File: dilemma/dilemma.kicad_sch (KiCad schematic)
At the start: 64 parts, among them J1 S3B-PH-SM4-TB(LF)(SN), J2 Serial, J3 BATTERY_CONN_DEANS, J5 S3B-PH-SM4-TB(LF)(SN), J7 trackball, SW1 SW_Push, SW10 SW_Push, SW11 SW_Push, SW12 SW_Push, SW13 SW_Push, SW14 SW_Push, SW15 SW_Push, SW16 SW_Push, SW17 SW_Push, SW2 SW_Push, SW26 SW_SPST, SW3 SW_Push, SW37 SW_SPST, SW4 SW_Push, SW5 SW_Push, SW6 SW_Push, SW7 SW_Push, SW8 SW_Push, SW9 SW_Push, U2 eliteC

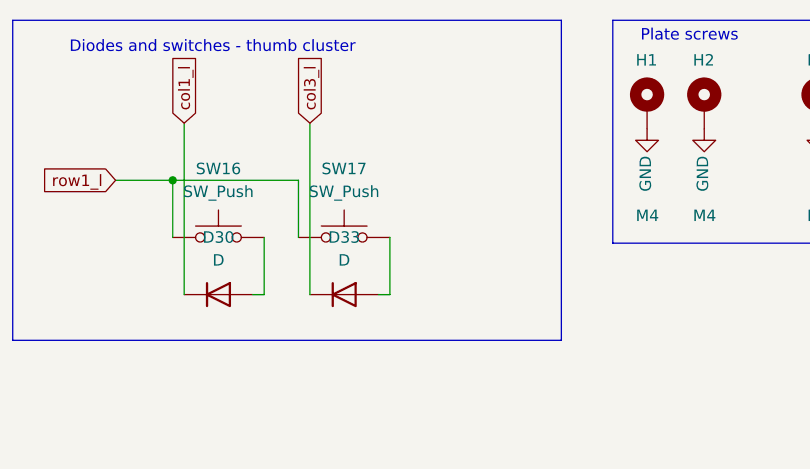
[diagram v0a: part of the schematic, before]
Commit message: Add thumb key
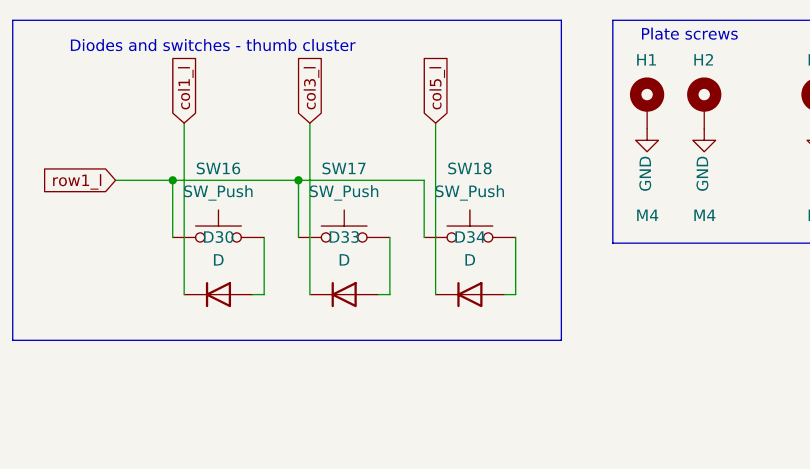
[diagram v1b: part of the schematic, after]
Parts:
- added D34: D, local-libraries:D_1206_handsolder_reversible, symbol Device:D
- added SW18: SW_Push, local-libraries:SW_MX_choc, symbol Switch:SW_Push
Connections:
- net col5_l: now also D34.1 (K)
- net row1_l: now also SW18.1
- new net: D34.2 (A), SW18.2
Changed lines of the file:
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@@
   (junction (at 109.22 45.72) (diameter 0) (color 0 0 0 0)
+  )
+  (junction (at 226.06 40.64) (diameter 0) (color 0 0 0 0)
   )
   (junction (at 212.09 40.64) (diameter 0) (color 0 0 0 0)
@@
     (stroke (width 0) (type default) (color 0 0 0 0))
   )
+  (wire (pts (xy 250.19 46.99) (xy 250.19 53.34))
+    (stroke (width 0) (type solid) (color 0 0 0 0))
+  )
   (wire (pts (xy 55.88 35.56) (xy 82.55 35.56))
     (stroke (width 0) (type default) (color 0 0 0 0))
@@
     (stroke (width 0) (type default) (color 0 0 0 0))
   )
+  (wire (pts (xy 250.19 53.34) (xy 248.92 53.34))
+    (stroke (width 0) (type solid) (color 0 0 0 0))
+  )
   (wire (pts (xy 308.61 111.76) (xy 311.785 111.76))
     (stroke (width 0) (type default) (color 0 0 0 0))
@@
     (stroke (width 0) (type default) (color 0 0 0 0))
   )
+  (wire (pts (xy 241.3 34.29) (xy 241.3 53.34))
+    (stroke (width 0) (type solid) (color 0 0 0 0))
+  )
+  (wire (pts (xy 226.06 40.64) (xy 240.03 40.64))
+    (stroke (width 0) (type solid) (color 0 0 0 0))
+  )
   (wire (pts (xy 154.94 48.26) (xy 158.75 48.26))
     (stroke (width 0) (type default) (color 0 0 0 0))
@@
   (wire (pts (xy 128.27 58.42) (xy 132.08 58.42))
     (stroke (width 0) (type default) (color 0 0 0 0))
+  )
+  (wire (pts (xy 240.03 40.64) (xy 240.03 46.99))
+    (stroke (width 0) (type solid) (color 0 0 0 0))
   )
   (wire (pts (xy 128.27 38.1) (xy 132.08 38.1))
@@
     )
   )
+  (global_label "col5_l" (shape input) (at 241.3 34.29 90)
+    (effects (font (size 1.27 1.27)) (justify left))
+    (property "Intersheet References" "${INTERSHEET_REFS}" (id 0) (at 96.52 3.81 0)
+      (effects (font (size 1.27 1.27)) hide)
+    )
+  )
   (global_label "bat_sw_l" (shape input) (at 177.8 99.06 180)
     (effects (font (size 1.27 1.27)) (justify right))
@@
     (pin "2")
   )
+  (symbol (lib_id "Device:D") (at 245.11 53.34 0) (unit 1)
+    (in_bom yes) (on_board yes)
+    (property "Reference" "D34" (id 0) (at 245.11 46.99 0))
+    (property "Value" "D" (id 1) (at 245.11 49.53 0))
+    (property "Footprint" "local-libraries:D_1206_handsolder_reversible" (id 2) (at 245.11 53.34 0)
+      (effects (font (size 1.27 1.27)) hide)
+    )
+    (property "Datasheet" "~" (id 3) (at 245.11 53.34 0)
+      (effects (font (size 1.27 1.27)) hide)
+    )
+    (pin "1")
+    (pin "2")
+  )
   (symbol (lib_id "Mechanical:MountingHole_Pad") (at 320.04 32.385 0) (unit 1)
     (in_bom yes) (on_board yes)
@@
     )
     (property "JLCPCB Part" "C26033" (id 5) (at 55.372 152.4 0)
+      (effects (font (size 1.27 1.27)) hide)
+    )
+    (pin "1")
+    (pin "2")
+  )
+  (symbol (lib_id "Switch:SW_Push") (at 245.11 46.99 0) (unit 1)
+    (in_bom yes) (on_board yes)
+    (property "Reference" "SW18" (id 0) (at 245.11 39.37 0))
+    (property "Value" "SW_Push" (id 1) (at 245.11 41.91 0))
+    (property "Footprint" "local-libraries:SW_MX_choc" (id 2) (at 245.11 41.91 0)
+      (effects (font (size 1.27 1.27)) hide)
+    )
+    (property "Datasheet" "~" (id 3) (at 245.11 41.91 0)
       (effects (font (size 1.27 1.27)) hide)
     )
@@
       (reference "D33") (unit 1) (value "D") (footprint "local-libraries:D_1206_handsolder_reversible")
     )
+    (path "/14dac5a2-a0ff-4444-afb5-3f69e91ff7db"
+      (reference "D34") (unit 1) (value "D") (footprint "local-libraries:D_1206_handsolder_reversible")
+    )
     (path "/66749c6a-b16f-43be-bab1-76caa7a8a44a"
       (reference "H1") (unit 1) (value "M4") (footprint "local-libraries:MountingHole_3mm_Pad_thin")
@@
       (reference "SW17") (unit 1) (value "SW_Push") (footprint "local-libraries:SW_MX_choc")
     )
+    (path "/2c60993d-fff3-4952-b82a-c33bf7f0fa97"
+      (reference "SW18") (unit 1) (value "SW_Push") (footprint "local-libraries:SW_MX_choc")
+    )
     (path "/bc6fb766-b233-4d2e-bea0-ce056a378236"

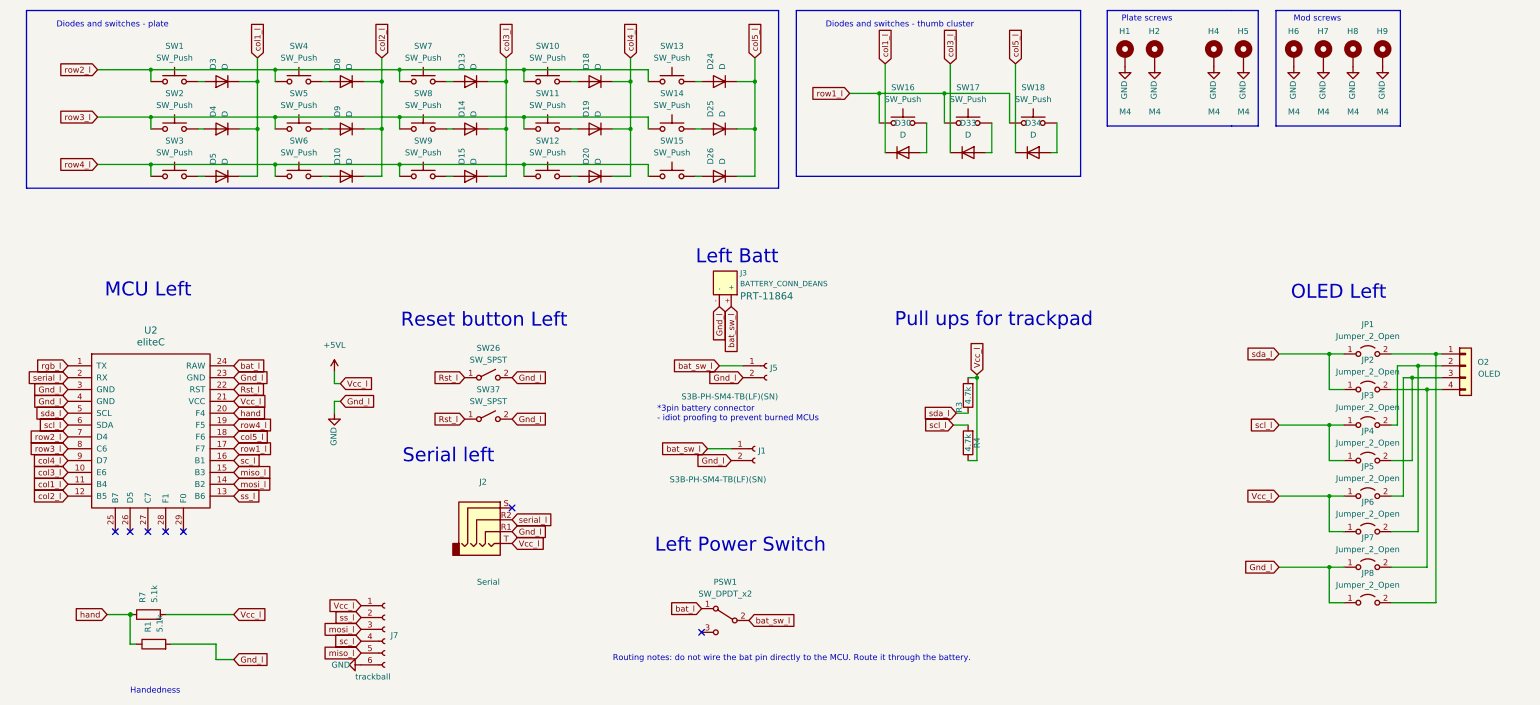
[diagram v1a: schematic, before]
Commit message: Create place for col6
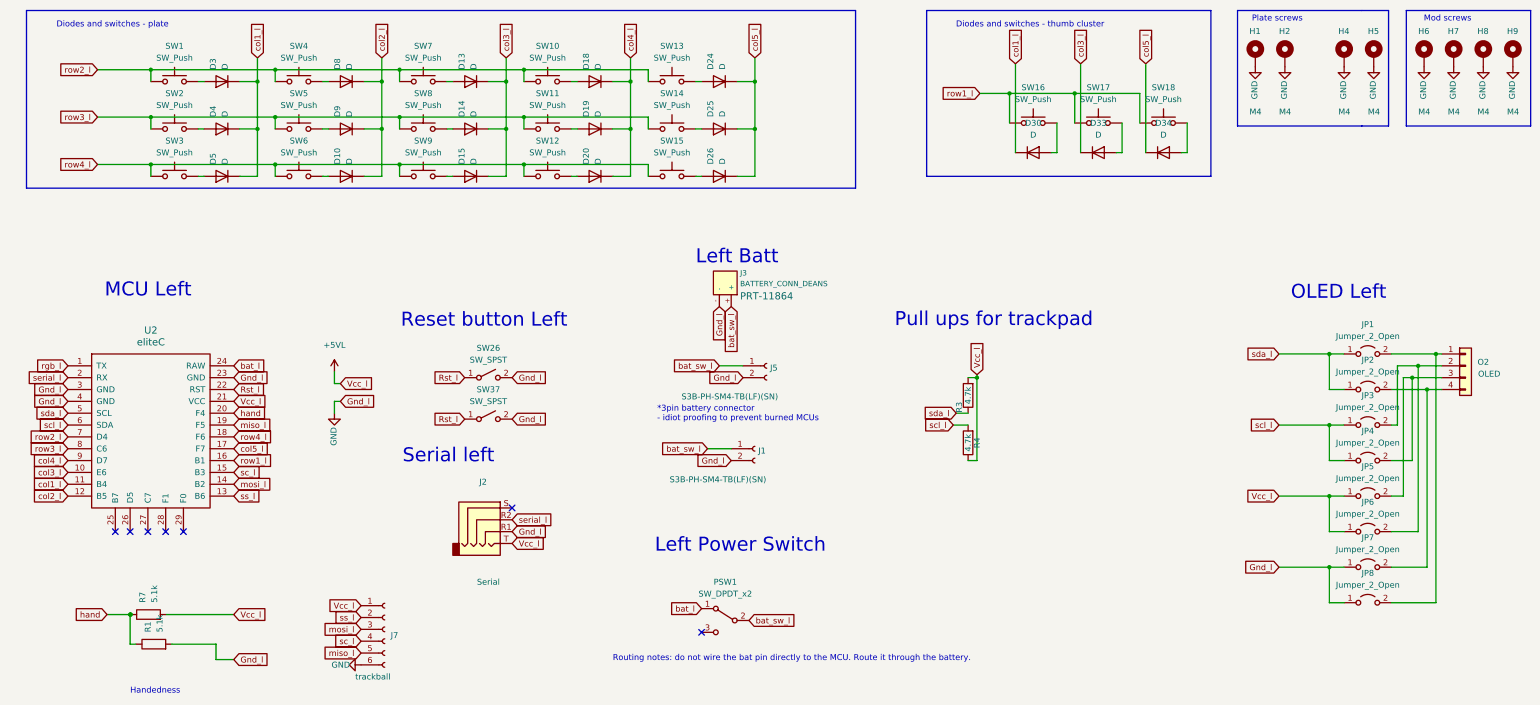
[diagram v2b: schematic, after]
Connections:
- net col5_l: now also U2.17 (F7); no longer U2.18 (F6)
- net miso_l: now also U2.19 (F5); no longer U2.15 (B3)
- net row1_l: now also U2.16 (B1); no longer U2.17 (F7)
- net row4_l: now also U2.18 (F6); no longer U2.19 (F5)
- net sc_l: now also U2.15 (B3); no longer U2.16 (B1)
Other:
- moved on the sheet: D30, D33, D34, H1, H2, H4, H5, H6, H7, H8, H9, SW16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

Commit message: Add 6th column
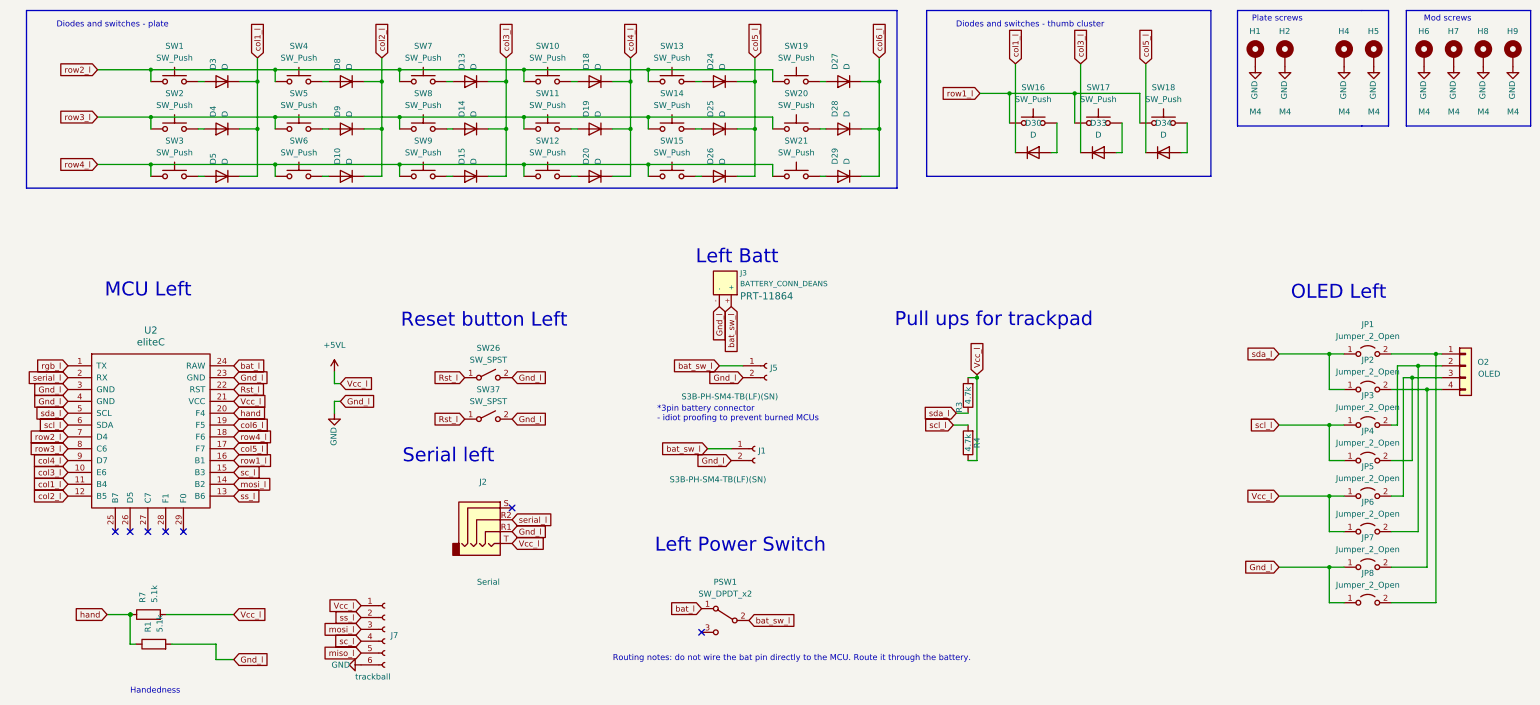
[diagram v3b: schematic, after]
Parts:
- added D27, D28, D29: D, local-libraries:D_1206_handsolder_reversible, symbol Device:D
- added SW19, SW20, SW21: SW_Push, local-libraries:SW_MX_choc, symbol Switch:SW_Push
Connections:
- net miso_l: no longer U2.19 (F5)
- net row2_l: now also SW19.1
- net row3_l: now also SW20.1
- net row4_l: now also SW21.1
- new net: D29.2 (A), SW21.2
- new net: D27.2 (A), SW19.2
- new net: D28.2 (A), SW20.2
- new net col6_l: D27.1 (K), D28.1 (K), D29.1 (K), U2.19 (F5)

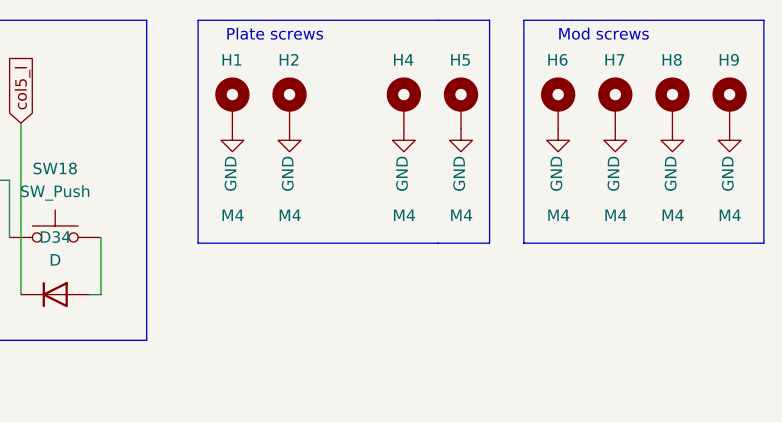
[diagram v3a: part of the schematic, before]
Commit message: Remove H4 hole
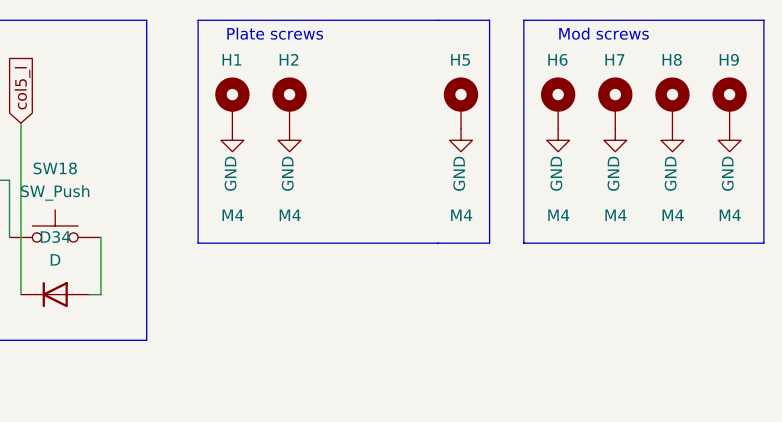
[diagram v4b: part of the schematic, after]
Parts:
- removed H4: M4, local-libraries:MountingHole_3mm_Pad_thin, symbol Mechanical:MountingHole_Pad
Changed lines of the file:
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@@
     (pin "2")
-  )
-  (symbol (lib_id "Mechanical:MountingHole_Pad") (at 311.785 32.385 0) (unit 1)
-    (in_bom yes) (on_board yes)
-    (property "Reference" "H4" (id 0) (at 310.515 27.305 0)
-      (effects (font (size 1.27 1.27)) (justify left))
-    )
-    (property "Value" "M4" (id 1) (at 310.515 44.577 0)
-      (effects (font (size 1.27 1.27)) (justify left))
-    )
-    (property "Footprint" "local-libraries:MountingHole_3mm_Pad_thin" (id 2) (at 311.785 32.385 0)
-      (effects (font (size 1.27 1.27)) hide)
-    )
-    (property "Datasheet" "~" (id 3) (at 311.785 32.385 0)
-      (effects (font (size 1.27 1.27)) hide)
-    )
-    (pin "1")
   )
   (symbol (lib_id "Switch:SW_Push") (at 114.3 48.26 0) (unit 1)
@@
     (pin "2")
   )
-  (symbol (lib_id "power:GND") (at 311.785 34.925 0) (unit 1)
-    (in_bom yes) (on_board yes)
-    (property "Reference" "#PWR0103" (id 0) (at 311.785 41.275 0)
-      (effects (font (size 1.27 1.27)) hide)
-    )
-    (property "Value" "GND" (id 1) (at 311.629 41.9099 90)
-      (effects (font (size 1.27 1.27)) (justify left))
-    )
-    (property "Footprint" "" (id 2) (at 311.785 34.925 0)
-      (effects (font (size 1.27 1.27)) hide)
-    )
-    (property "Datasheet" "" (id 3) (at 311.785 34.925 0)
-      (effects (font (size 1.27 1.27)) hide)
-    )
-    (pin "1")
-  )
   (symbol (lib_id "power:GND") (at 328.93 34.925 0) (unit 1)
     (in_bom yes) (on_board yes)
@@
       (reference "#PWR0102") (unit 1) (value "GND") (footprint "")
     )
-    (path "/fb97fa38-e913-4813-bbb6-ec56f9359020"
-      (reference "#PWR0103") (unit 1) (value "GND") (footprint "")
-    )
     (path "/9a573a5f-16ed-4bac-a9aa-25b5d86e5dd3"
       (reference "#PWR0104") (unit 1) (value "GND") (footprint "")
@@
       (reference "H2") (unit 1) (value "M4") (footprint "local-libraries:MountingHole_3mm_Pad_thin")
     )
-    (path "/eab541c6-214e-4bdc-a65e-96cf56f5a486"
-      (reference "H4") (unit 1) (value "M4") (footprint "local-libraries:MountingHole_3mm_Pad_thin")
-    )
     (path "/2da60390-ff21-4437-82a4-3e8bcdc893cf"

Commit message: Revert "Remove H4 hole"
This reverts commit eafe3389c8530ed03ec8ad130b3a2f53ccdd09a2.
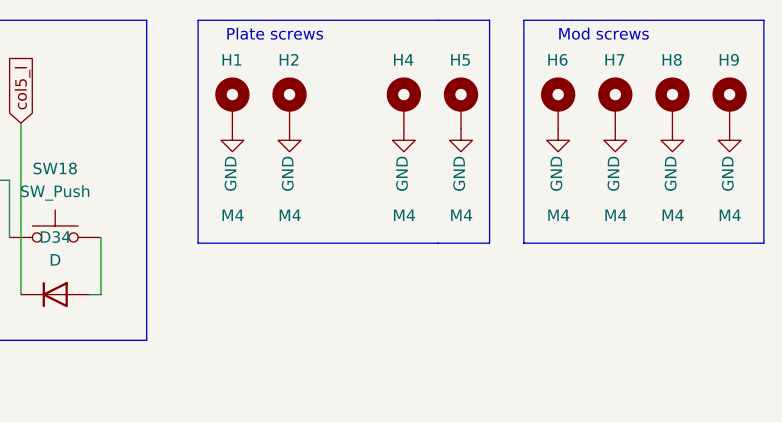
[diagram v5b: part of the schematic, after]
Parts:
- added H4: M4, local-libraries:MountingHole_3mm_Pad_thin, symbol Mechanical:MountingHole_Pad
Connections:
- net GND: now also H4.1
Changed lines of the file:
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@@
     (pin "2")
+  )
+  (symbol (lib_id "Mechanical:MountingHole_Pad") (at 311.785 32.385 0) (unit 1)
+    (in_bom yes) (on_board yes)
+    (property "Reference" "H4" (id 0) (at 310.515 27.305 0)
+      (effects (font (size 1.27 1.27)) (justify left))
+    )
+    (property "Value" "M4" (id 1) (at 310.515 44.577 0)
+      (effects (font (size 1.27 1.27)) (justify left))
+    )
+    (property "Footprint" "local-libraries:MountingHole_3mm_Pad_thin" (id 2) (at 311.785 32.385 0)
+      (effects (font (size 1.27 1.27)) hide)
+    )
+    (property "Datasheet" "~" (id 3) (at 311.785 32.385 0)
+      (effects (font (size 1.27 1.27)) hide)
+    )
+    (pin "1")
   )
   (symbol (lib_id "Switch:SW_Push") (at 114.3 48.26 0) (unit 1)
@@
     (pin "2")
   )
+  (symbol (lib_id "power:GND") (at 311.785 34.925 0) (unit 1)
+    (in_bom yes) (on_board yes)
+    (property "Reference" "#PWR0103" (id 0) (at 311.785 41.275 0)
+      (effects (font (size 1.27 1.27)) hide)
+    )
+    (property "Value" "GND" (id 1) (at 311.629 41.9099 90)
+      (effects (font (size 1.27 1.27)) (justify left))
+    )
+    (property "Footprint" "" (id 2) (at 311.785 34.925 0)
+      (effects (font (size 1.27 1.27)) hide)
+    )
+    (property "Datasheet" "" (id 3) (at 311.785 34.925 0)
+      (effects (font (size 1.27 1.27)) hide)
+    )
+    (pin "1")
+  )
   (symbol (lib_id "power:GND") (at 328.93 34.925 0) (unit 1)
     (in_bom yes) (on_board yes)
@@
       (reference "#PWR0102") (unit 1) (value "GND") (footprint "")
     )
+    (path "/fb97fa38-e913-4813-bbb6-ec56f9359020"
+      (reference "#PWR0103") (unit 1) (value "GND") (footprint "")
+    )
     (path "/9a573a5f-16ed-4bac-a9aa-25b5d86e5dd3"
       (reference "#PWR0104") (unit 1) (value "GND") (footprint "")
@@
       (reference "H2") (unit 1) (value "M4") (footprint "local-libraries:MountingHole_3mm_Pad_thin")
     )
+    (path "/eab541c6-214e-4bdc-a65e-96cf56f5a486"
+      (reference "H4") (unit 1) (value "M4") (footprint "local-libraries:MountingHole_3mm_Pad_thin")
+    )
     (path "/2da60390-ff21-4437-82a4-3e8bcdc893cf"
